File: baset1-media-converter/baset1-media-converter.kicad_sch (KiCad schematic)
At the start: 28 parts, among them J1 CONN_01X05, M1 LOGO, M2 LOGO, M3 LOGO, U1 STM32F031-QFN28

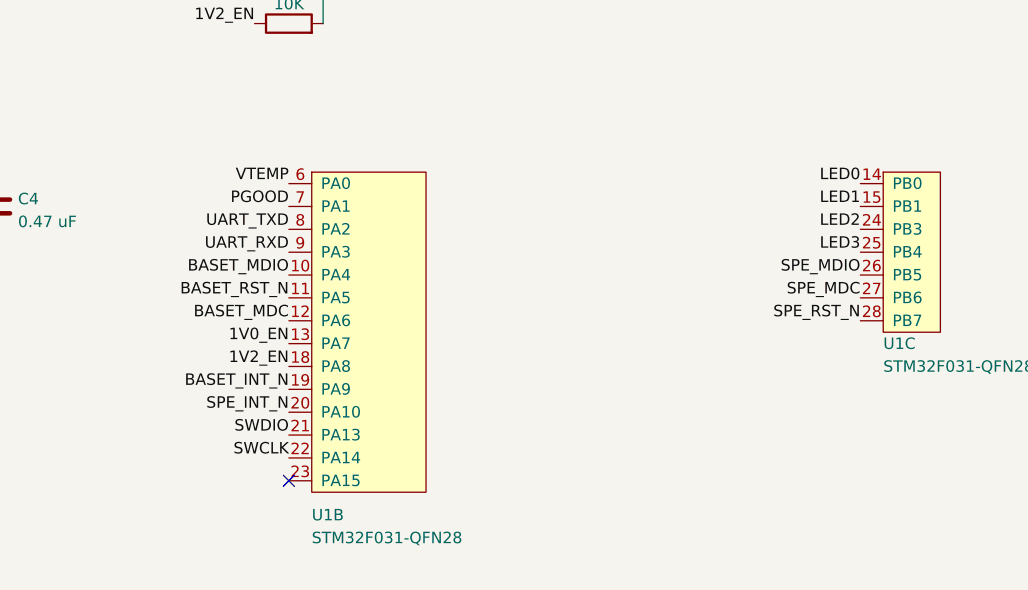
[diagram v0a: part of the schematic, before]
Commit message: Continued layout on media converter
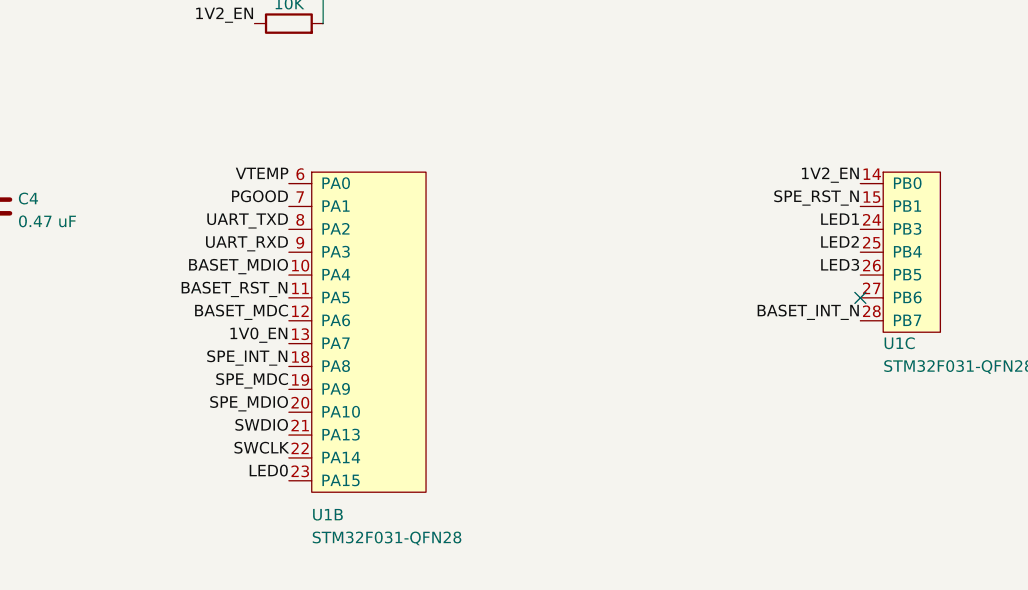
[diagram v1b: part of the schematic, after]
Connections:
- net 1V2_EN: now also U1.14 (PB0); no longer U1.18 (PA8)
- net BASET_INT_N: now also U1.28 (PB7); no longer U1.19 (PA9)
- net LED0: now also U1.23 (PA15); no longer U1.14 (PB0)
- net LED1: now also U1.24 (PB3); no longer U1.15 (PB1)
- net LED2: now also U1.25 (PB4); no longer U1.24 (PB3)
- net LED3: now also U1.26 (PB5); no longer U1.25 (PB4)
- net SPE_INT_N: now also U1.18 (PA8); no longer U1.20 (PA10)
- net SPE_MDC: now also U1.19 (PA9); no longer U1.27 (PB6)
- net SPE_MDIO: now also U1.20 (PA10); no longer U1.26 (PB5)
- net SPE_RST_N: now also U1.15 (PB1); no longer U1.28 (PB7)
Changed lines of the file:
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@@
   (title_block
     (title "BaseT to BaseT1 Media Converter")
-    (date "2024-01-25")
+    (date "2024-01-27")
     (rev "0.1")
     (company "Antikernel Labs")
@@
   (no_connect (at 132.08 24.13))
   (no_connect (at 49.53 252.73))
-  (no_connect (at 139.7 267.97))
+  (no_connect (at 203.2 247.65))
   (wire (pts (xy 49.53 90.17) (xy 77.47 90.17))
     (stroke (width 0) (type default) (color 0 0 0 0))
@@
     (effects (font (size 1.27 1.27)) (justify right bottom))
   )
-  (label "1V2_EN" (at 139.7 255.27 180)
-    (effects (font (size 1.27 1.27)) (justify right bottom))
-  )
-  (label "SPE_INT_N" (at 139.7 260.35 180)
+  (label "1V2_EN" (at 203.2 234.95 180)
+    (effects (font (size 1.27 1.27)) (justify right bottom))
+  )
+  (label "SPE_INT_N" (at 139.7 255.27 180)
     (effects (font (size 1.27 1.27)) (justify right bottom))
   )
@@
     (effects (font (size 1.27 1.27)) (justify right bottom))
   )
-  (label "BASET_INT_N" (at 139.7 257.81 180)
-    (effects (font (size 1.27 1.27)) (justify right bottom))
-  )
-  (label "SPE_MDIO" (at 203.2 245.11 180)
+  (label "BASET_INT_N" (at 203.2 250.19 180)
+    (effects (font (size 1.27 1.27)) (justify right bottom))
+  )
+  (label "SPE_MDIO" (at 139.7 260.35 180)
     (effects (font (size 1.27 1.27)) (justify right bottom))
   )
@@
     (effects (font (size 1.27 1.27)) (justify left bottom))
   )
-  (label "LED2" (at 203.2 240.03 180)
+  (label "LED2" (at 203.2 242.57 180)
     (effects (font (size 1.27 1.27)) (justify right bottom))
   )
@@
     (effects (font (size 1.27 1.27)) (justify right bottom))
   )
-  (label "SPE_RST_N" (at 203.2 250.19 180)
+  (label "SPE_RST_N" (at 203.2 237.49 180)
     (effects (font (size 1.27 1.27)) (justify right bottom))
   )
@@
     (effects (font (size 1.27 1.27)) (justify right bottom))
   )
-  (label "LED0" (at 203.2 234.95 180)
+  (label "LED0" (at 139.7 267.97 180)
     (effects (font (size 1.27 1.27)) (justify right bottom))
   )
@@
     (effects (font (size 1.27 1.27)) (justify left bottom))
   )
-  (label "LED1" (at 203.2 237.49 180)
+  (label "LED1" (at 203.2 240.03 180)
     (effects (font (size 1.27 1.27)) (justify right bottom))
   )
@@
     (effects (font (size 1.27 1.27)) (justify right bottom))
   )
-  (label "LED3" (at 203.2 242.57 180)
+  (label "LED3" (at 203.2 245.11 180)
     (effects (font (size 1.27 1.27)) (justify right bottom))
   )
@@
     (effects (font (size 1.27 1.27)) (justify right bottom))
   )
-  (label "SPE_MDC" (at 203.2 247.65 180)
+  (label "SPE_MDC" (at 139.7 257.81 180)
     (effects (font (size 1.27 1.27)) (justify right bottom))
   )
@@
       (reference "TP15") (unit 1) (value "TESTCLIP") (footprint "azonenberg_pcb:TESTPOINT_SMT_KEYSTONE_5016")
     )
-    (path "/2b314ace-fee4-4d04-b15a-691b3c91b027/bef7ed6a-cc7a-4be1-b4ad-27a0f0469392"
-      (reference "TP16") (unit 1) (value "U.FL") (footprint "azonenberg_pcb:CONN_U.FL_TE_1909763-1")
-    )
     (path "/335dd89e-09bc-42e0-811e-78063fda6d1c"

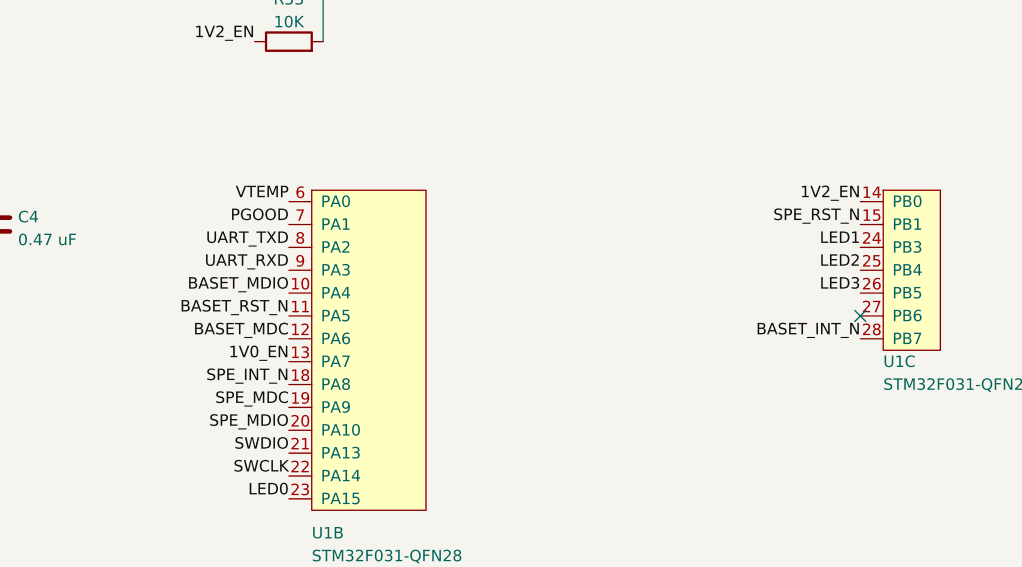
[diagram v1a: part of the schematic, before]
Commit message: Updating file: baset1-media-converter.kicad_pcb with current fully routed design
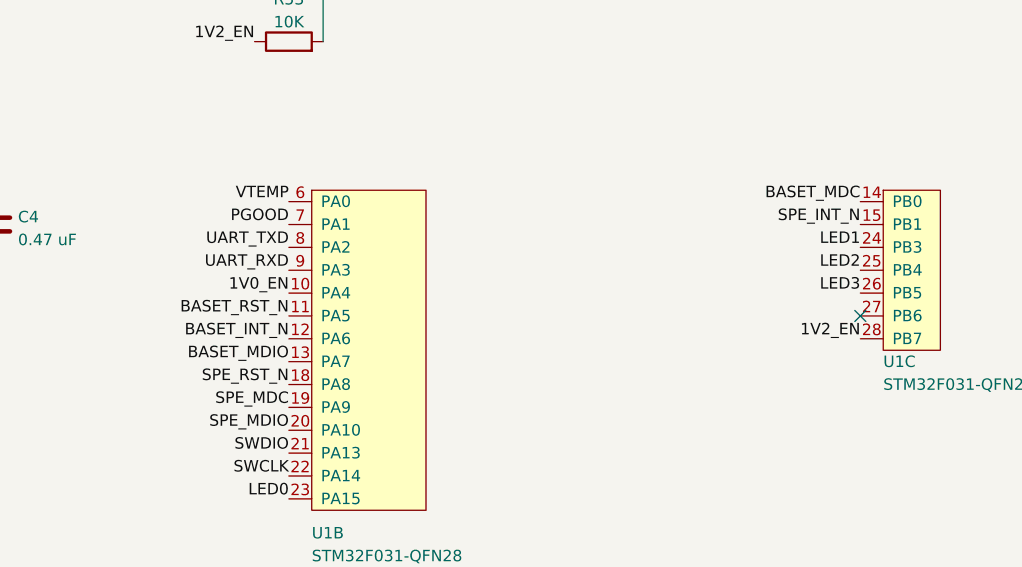
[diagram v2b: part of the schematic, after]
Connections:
- net 1V0_EN: now also U1.10 (PA4); no longer U1.13 (PA7)
- net 1V2_EN: now also U1.28 (PB7); no longer U1.14 (PB0)
- net BASET_INT_N: now also U1.12 (PA6); no longer U1.28 (PB7)
- net BASET_MDC: now also U1.14 (PB0); no longer U1.12 (PA6)
- net BASET_MDIO: now also U1.13 (PA7); no longer U1.10 (PA4)
- net SPE_INT_N: now also U1.15 (PB1); no longer U1.18 (PA8)
- net SPE_RST_N: now also U1.18 (PA8); no longer U1.15 (PB1)
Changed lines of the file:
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@@
   (title_block
     (title "BaseT to BaseT1 Media Converter")
-    (date "2024-01-27")
+    (date "2024-01-28")
     (rev "0.1")
     (company "Antikernel Labs")
@@
     (effects (font (size 1.27 1.27)) (justify right bottom))
   )
-  (label "1V0_EN" (at 139.7 252.73 180)
-    (effects (font (size 1.27 1.27)) (justify right bottom))
-  )
-  (label "1V2_EN" (at 203.2 234.95 180)
-    (effects (font (size 1.27 1.27)) (justify right bottom))
-  )
-  (label "SPE_INT_N" (at 139.7 255.27 180)
+  (label "1V0_EN" (at 139.7 245.11 180)
+    (effects (font (size 1.27 1.27)) (justify right bottom))
+  )
+  (label "1V2_EN" (at 203.2 250.19 180)
+    (effects (font (size 1.27 1.27)) (justify right bottom))
+  )
+  (label "SPE_INT_N" (at 203.2 237.49 180)
     (effects (font (size 1.27 1.27)) (justify right bottom))
   )
@@
     (effects (font (size 1.27 1.27)) (justify right bottom))
   )
-  (label "BASET_INT_N" (at 203.2 250.19 180)
+  (label "BASET_INT_N" (at 139.7 250.19 180)
     (effects (font (size 1.27 1.27)) (justify right bottom))
   )
@@
     (effects (font (size 1.27 1.27)) (justify right bottom))
   )
-  (label "SPE_RST_N" (at 203.2 237.49 180)
+  (label "SPE_RST_N" (at 139.7 255.27 180)
     (effects (font (size 1.27 1.27)) (justify right bottom))
   )
@@
     (effects (font (size 1.27 1.27)) (justify left bottom))
   )
-  (label "BASET_MDIO" (at 139.7 245.11 180)
+  (label "BASET_MDIO" (at 139.7 252.73 180)
     (effects (font (size 1.27 1.27)) (justify right bottom))
   )
@@
     (effects (font (size 1.27 1.27)) (justify right bottom))
   )
-  (label "BASET_MDC" (at 139.7 250.19 180)
-    (effects (font (size 1.27 1.27)) (justify right bottom))
-  )
+  (label "BASET_MDC" (at 203.2 234.95 180)
+    (effects (font (size 1.27 1.27)) (justify right bottom))
+  )

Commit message: Final v0.1 media converter design after layout review
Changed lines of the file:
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@@
     (pin "19")
     (pin "20")
-    (pin "21")
-    (pin "22")
+    (pin "21" (alternate "SWDIO"))
+    (pin "22" (alternate "SWCLK"))
     (pin "23")
-    (pin "6")
+    (pin "6" (alternate "ADC_IN0"))
     (pin "7")
-    (pin "8")
-    (pin "9")
+    (pin "8" (alternate "USART1_TX"))
+    (pin "9" (alternate "USART1_RX"))
     (pin "14")
     (pin "15")
@@
     (pin "19")
     (pin "20")
-    (pin "21")
-    (pin "22")
+    (pin "21" (alternate "SWDIO"))
+    (pin "22" (alternate "SWCLK"))
     (pin "23")
-    (pin "6")
+    (pin "6" (alternate "ADC_IN0"))
     (pin "7")
-    (pin "8")
-    (pin "9")
+    (pin "8" (alternate "USART1_TX"))
+    (pin "9" (alternate "USART1_RX"))
     (pin "14")
     (pin "15")
@@
     (pin "19")
     (pin "20")
-    (pin "21")
-    (pin "22")
+    (pin "21" (alternate "SWDIO"))
+    (pin "22" (alternate "SWCLK"))
     (pin "23")
-    (pin "6")
+    (pin "6" (alternate "ADC_IN0"))
     (pin "7")
-    (pin "8")
-    (pin "9")
+    (pin "8" (alternate "USART1_TX"))
+    (pin "9" (alternate "USART1_RX"))
     (pin "14")
     (pin "15")
